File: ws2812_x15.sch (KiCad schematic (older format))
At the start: 16 parts

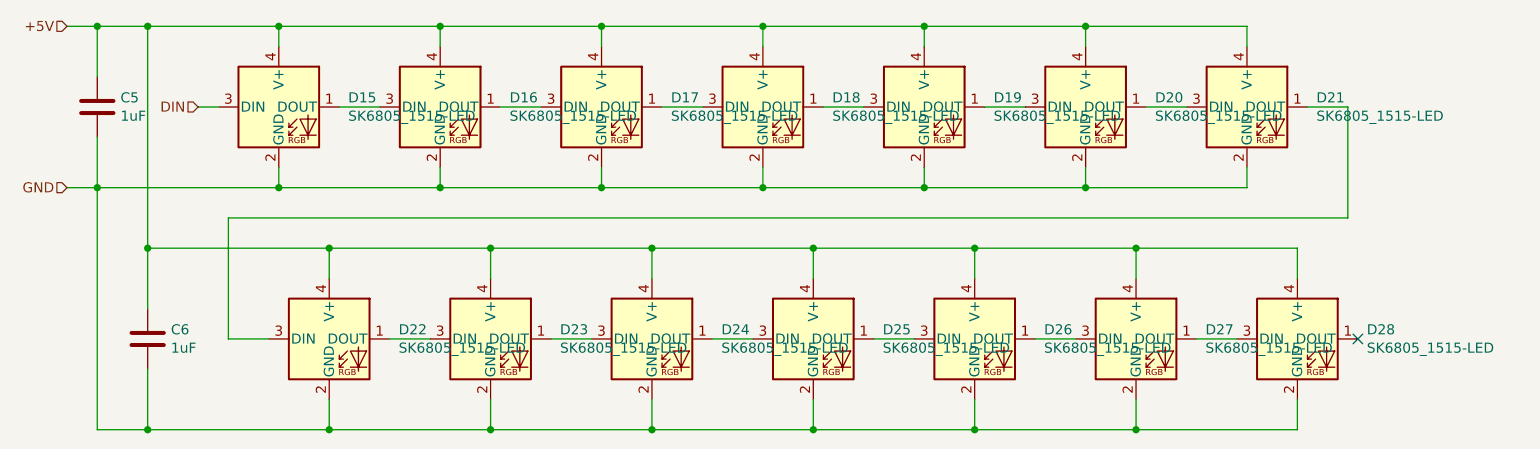
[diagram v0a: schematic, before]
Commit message: Update with changes to use attiny13a only
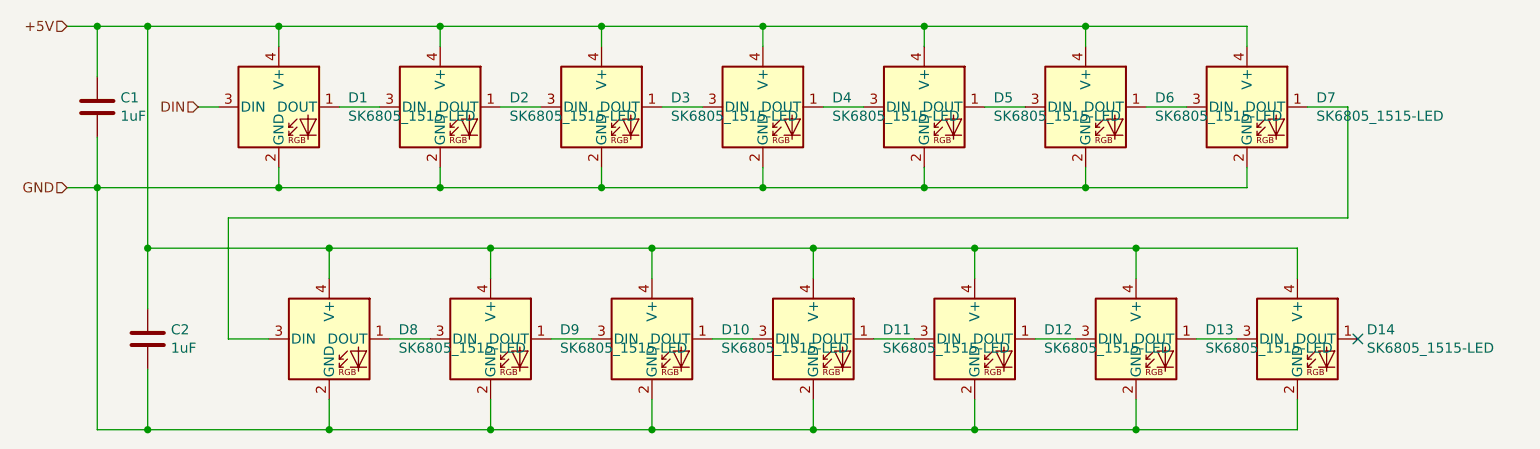
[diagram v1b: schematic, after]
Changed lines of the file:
@@
 $Descr A4 11693 8268
 encoding utf-8
-Sheet 1 3
+Sheet 2 3
 Title ""
 Date ""
@@
 AR Path="/5FC2CFBE/5FBCF9D4" Ref="D1"  Part="1"
 AR Path="/5FC2D616/5FBCF9D4" Ref="D15"  Part="1"
-AR Path="/5FC48FEB/5FBCF9D4" Ref="D?"  Part="1"
-AR Path="/5FC491DE/5FBCF9D4" Ref="D?"  Part="1"
-F 0 "D15" H 2794 1946 50  0000 L CNN
+AR Path="/5FC48FEB/5FBCF9D4" Ref="D1"  Part="1"
+AR Path="/5FC491DE/5FBCF9D4" Ref="D15"  Part="1"
+F 0 "D1" H 2794 1946 50  0000 L CNN
 F 1 "SK6805_1515-LED" H 2794 1855 50  0000 L CNN
 F 2 "LED_SMD:LED_SK6805_PLCC4_1.5x1.5mm_P0.65mm" H 2500 1600 50  0001 L TNN
@@
 AR Path="/5FC2CFBE/5FBD0769" Ref="C3"  Part="1"
 AR Path="/5FC2D616/5FBD0769" Ref="C5"  Part="1"
-AR Path="/5FC48FEB/5FBD0769" Ref="C?"  Part="1"
-AR Path="/5FC491DE/5FBD0769" Ref="C?"  Part="1"
-F 0 "C5" H 1665 1946 50  0000 L CNN
+AR Path="/5FC48FEB/5FBD0769" Ref="C1"  Part="1"
+AR Path="/5FC491DE/5FBD0769" Ref="C3"  Part="1"
+F 0 "C1" H 1665 1946 50  0000 L CNN
 F 1 "1uF" H 1665 1855 50  0000 L CNN
 F 2 "Capacitor_SMD:C_0603_1608Metric" H 1588 1750 50  0001 C CNN
@@
 AR Path="/5FC2CFBE/5FBD28C7" Ref="D2"  Part="1"
 AR Path="/5FC2D616/5FBD28C7" Ref="D16"  Part="1"
-AR Path="/5FC48FEB/5FBD28C7" Ref="D?"  Part="1"
-AR Path="/5FC491DE/5FBD28C7" Ref="D?"  Part="1"
-F 0 "D16" H 3594 1946 50  0000 L CNN
+AR Path="/5FC48FEB/5FBD28C7" Ref="D2"  Part="1"
+AR Path="/5FC491DE/5FBD28C7" Ref="D16"  Part="1"
+F 0 "D2" H 3594 1946 50  0000 L CNN
 F 1 "SK6805_1515-LED" H 3594 1855 50  0000 L CNN
 F 2 "LED_SMD:LED_SK6805_PLCC4_1.5x1.5mm_P0.65mm" H 3300 1600 50  0001 L TNN
@@
 AR Path="/5FC2CFBE/5FBD39DB" Ref="D3"  Part="1"
 AR Path="/5FC2D616/5FBD39DB" Ref="D17"  Part="1"
-AR Path="/5FC48FEB/5FBD39DB" Ref="D?"  Part="1"
-AR Path="/5FC491DE/5FBD39DB" Ref="D?"  Part="1"
-F 0 "D17" H 4394 1946 50  0000 L CNN
+AR Path="/5FC48FEB/5FBD39DB" Ref="D3"  Part="1"
+AR Path="/5FC491DE/5FBD39DB" Ref="D17"  Part="1"
+F 0 "D3" H 4394 1946 50  0000 L CNN
 F 1 "SK6805_1515-LED" H 4394 1855 50  0000 L CNN
 F 2 "LED_SMD:LED_SK6805_PLCC4_1.5x1.5mm_P0.65mm" H 4100 1600 50  0001 L TNN
@@
 AR Path="/5FC2CFBE/5FBD39E1" Ref="D4"  Part="1"
 AR Path="/5FC2D616/5FBD39E1" Ref="D18"  Part="1"
-AR Path="/5FC48FEB/5FBD39E1" Ref="D?"  Part="1"
-AR Path="/5FC491DE/5FBD39E1" Ref="D?"  Part="1"
-F 0 "D18" H 5194 1946 50  0000 L CNN
+AR Path="/5FC48FEB/5FBD39E1" Ref="D4"  Part="1"
+AR Path="/5FC491DE/5FBD39E1" Ref="D18"  Part="1"
+F 0 "D4" H 5194 1946 50  0000 L CNN
 F 1 "SK6805_1515-LED" H 5194 1855 50  0000 L CNN
 F 2 "LED_SMD:LED_SK6805_PLCC4_1.5x1.5mm_P0.65mm" H 4900 1600 50  0001 L TNN
@@
 AR Path="/5FC2CFBE/5FBD73F9" Ref="D5"  Part="1"
 AR Path="/5FC2D616/5FBD73F9" Ref="D19"  Part="1"
-AR Path="/5FC48FEB/5FBD73F9" Ref="D?"  Part="1"
-AR Path="/5FC491DE/5FBD73F9" Ref="D?"  Part="1"
-F 0 "D19" H 5994 1946 50  0000 L CNN
+AR Path="/5FC48FEB/5FBD73F9" Ref="D5"  Part="1"
+AR Path="/5FC491DE/5FBD73F9" Ref="D19"  Part="1"
+F 0 "D5" H 5994 1946 50  0000 L CNN
 F 1 "SK6805_1515-LED" H 5994 1855 50  0000 L CNN
 F 2 "LED_SMD:LED_SK6805_PLCC4_1.5x1.5mm_P0.65mm" H 5700 1600 50  0001 L TNN
@@
 AR Path="/5FC2CFBE/5FBD73FF" Ref="D6"  Part="1"
 AR Path="/5FC2D616/5FBD73FF" Ref="D20"  Part="1"
-AR Path="/5FC48FEB/5FBD73FF" Ref="D?"  Part="1"
-AR Path="/5FC491DE/5FBD73FF" Ref="D?"  Part="1"
-F 0 "D20" H 6794 1946 50  0000 L CNN
+AR Path="/5FC48FEB/5FBD73FF" Ref="D6"  Part="1"
+AR Path="/5FC491DE/5FBD73FF" Ref="D20"  Part="1"
+F 0 "D6" H 6794 1946 50  0000 L CNN
 F 1 "SK6805_1515-LED" H 6794 1855 50  0000 L CNN
 F 2 "LED_SMD:LED_SK6805_PLCC4_1.5x1.5mm_P0.65mm" H 6500 1600 50  0001 L TNN
@@
 AR Path="/5FC2CFBE/5FBD7405" Ref="D7"  Part="1"
 AR Path="/5FC2D616/5FBD7405" Ref="D21"  Part="1"
-AR Path="/5FC48FEB/5FBD7405" Ref="D?"  Part="1"
-AR Path="/5FC491DE/5FBD7405" Ref="D?"  Part="1"
-F 0 "D21" H 7594 1946 50  0000 L CNN
+AR Path="/5FC48FEB/5FBD7405" Ref="D7"  Part="1"
+AR Path="/5FC491DE/5FBD7405" Ref="D21"  Part="1"
+F 0 "D7" H 7594 1946 50  0000 L CNN
 F 1 "SK6805_1515-LED" H 7594 1855 50  0000 L CNN
 F 2 "LED_SMD:LED_SK6805_PLCC4_1.5x1.5mm_P0.65mm" H 7300 1600 50  0001 L TNN
@@
 AR Path="/5FC2CFBE/5FBDBDCA" Ref="D8"  Part="1"
 AR Path="/5FC2D616/5FBDBDCA" Ref="D22"  Part="1"
-AR Path="/5FC48FEB/5FBDBDCA" Ref="D?"  Part="1"
-AR Path="/5FC491DE/5FBDBDCA" Ref="D?"  Part="1"
-F 0 "D22" H 3044 3096 50  0000 L CNN
+AR Path="/5FC48FEB/5FBDBDCA" Ref="D8"  Part="1"
+AR Path="/5FC491DE/5FBDBDCA" Ref="D22"  Part="1"
+F 0 "D8" H 3044 3096 50  0000 L CNN
 F 1 "SK6805_1515-LED" H 3044 3005 50  0000 L CNN
 F 2 "LED_SMD:LED_SK6805_PLCC4_1.5x1.5mm_P0.65mm" H 2750 2750 50  0001 L TNN
@@
 AR Path="/5FC2CFBE/5FBDBDD0" Ref="D9"  Part="1"
 AR Path="/5FC2D616/5FBDBDD0" Ref="D23"  Part="1"
-AR Path="/5FC48FEB/5FBDBDD0" Ref="D?"  Part="1"
-AR Path="/5FC491DE/5FBDBDD0" Ref="D?"  Part="1"
-F 0 "D23" H 3844 3096 50  0000 L CNN
+AR Path="/5FC48FEB/5FBDBDD0" Ref="D9"  Part="1"
+AR Path="/5FC491DE/5FBDBDD0" Ref="D23"  Part="1"
+F 0 "D9" H 3844 3096 50  0000 L CNN
 F 1 "SK6805_1515-LED" H 3844 3005 50  0000 L CNN
 F 2 "LED_SMD:LED_SK6805_PLCC4_1.5x1.5mm_P0.65mm" H 3550 2750 50  0001 L TNN
@@
 AR Path="/5FC2CFBE/5FBDBDD6" Ref="D10"  Part="1"
 AR Path="/5FC2D616/5FBDBDD6" Ref="D24"  Part="1"
-AR Path="/5FC48FEB/5FBDBDD6" Ref="D?"  Part="1"
-AR Path="/5FC491DE/5FBDBDD6" Ref="D?"  Part="1"
-F 0 "D24" H 4644 3096 50  0000 L CNN
+AR Path="/5FC48FEB/5FBDBDD6" Ref="D10"  Part="1"
+AR Path="/5FC491DE/5FBDBDD6" Ref="D24"  Part="1"
+F 0 "D10" H 4644 3096 50  0000 L CNN
 F 1 "SK6805_1515-LED" H 4644 3005 50  0000 L CNN
 F 2 "LED_SMD:LED_SK6805_PLCC4_1.5x1.5mm_P0.65mm" H 4350 2750 50  0001 L TNN
@@
 AR Path="/5FC2CFBE/5FBDBDDC" Ref="D11"  Part="1"
 AR Path="/5FC2D616/5FBDBDDC" Ref="D25"  Part="1"
-AR Path="/5FC48FEB/5FBDBDDC" Ref="D?"  Part="1"
-AR Path="/5FC491DE/5FBDBDDC" Ref="D?"  Part="1"
-F 0 "D25" H 5444 3096 50  0000 L CNN
+AR Path="/5FC48FEB/5FBDBDDC" Ref="D11"  Part="1"
+AR Path="/5FC491DE/5FBDBDDC" Ref="D25"  Part="1"
+F 0 "D11" H 5444 3096 50  0000 L CNN
 F 1 "SK6805_1515-LED" H 5444 3005 50  0000 L CNN
 F 2 "LED_SMD:LED_SK6805_PLCC4_1.5x1.5mm_P0.65mm" H 5150 2750 50  0001 L TNN
@@
 AR Path="/5FC2CFBE/5FBDBDE2" Ref="D12"  Part="1"
 AR Path="/5FC2D616/5FBDBDE2" Ref="D26"  Part="1"
-AR Path="/5FC48FEB/5FBDBDE2" Ref="D?"  Part="1"
-AR Path="/5FC491DE/5FBDBDE2" Ref="D?"  Part="1"
-F 0 "D26" H 6244 3096 50  0000 L CNN
+AR Path="/5FC48FEB/5FBDBDE2" Ref="D12"  Part="1"
+AR Path="/5FC491DE/5FBDBDE2" Ref="D26"  Part="1"
+F 0 "D12" H 6244 3096 50  0000 L CNN
 F 1 "SK6805_1515-LED" H 6244 3005 50  0000 L CNN
 F 2 "LED_SMD:LED_SK6805_PLCC4_1.5x1.5mm_P0.65mm" H 5950 2750 50  0001 L TNN
@@
 AR Path="/5FC2CFBE/5FBDBDE8" Ref="D13"  Part="1"
 AR Path="/5FC2D616/5FBDBDE8" Ref="D27"  Part="1"
-AR Path="/5FC48FEB/5FBDBDE8" Ref="D?"  Part="1"
-AR Path="/5FC491DE/5FBDBDE8" Ref="D?"  Part="1"
-F 0 "D27" H 7044 3096 50  0000 L CNN
+AR Path="/5FC48FEB/5FBDBDE8" Ref="D13"  Part="1"
+AR Path="/5FC491DE/5FBDBDE8" Ref="D27"  Part="1"
+F 0 "D13" H 7044 3096 50  0000 L CNN
 F 1 "SK6805_1515-LED" H 7044 3005 50  0000 L CNN
 F 2 "LED_SMD:LED_SK6805_PLCC4_1.5x1.5mm_P0.65mm" H 6750 2750 50  0001 L TNN
@@
 AR Path="/5FC2CFBE/5FBDBDEE" Ref="D14"  Part="1"
 AR Path="/5FC2D616/5FBDBDEE" Ref="D28"  Part="1"
-AR Path="/5FC48FEB/5FBDBDEE" Ref="D?"  Part="1"
-AR Path="/5FC491DE/5FBDBDEE" Ref="D?"  Part="1"
-F 0 "D28" H 7844 3096 50  0000 L CNN
+AR Path="/5FC48FEB/5FBDBDEE" Ref="D14"  Part="1"
+AR Path="/5FC491DE/5FBDBDEE" Ref="D28"  Part="1"
+F 0 "D14" H 7844 3096 50  0000 L CNN
 F 1 "SK6805_1515-LED" H 7844 3005 50  0000 L CNN
 F 2 "LED_SMD:LED_SK6805_PLCC4_1.5x1.5mm_P0.65mm" H 7550 2750 50  0001 L TNN
@@
 AR Path="/5FC2CFBE/5FBDD238" Ref="C4"  Part="1"
 AR Path="/5FC2D616/5FBDD238" Ref="C6"  Part="1"
-AR Path="/5FC48FEB/5FBDD238" Ref="C?"  Part="1"
-AR Path="/5FC491DE/5FBDD238" Ref="C?"  Part="1"
-F 0 "C6" H 1915 3096 50  0000 L CNN
+AR Path="/5FC48FEB/5FBDD238" Ref="C2"  Part="1"
+AR Path="/5FC491DE/5FBDD238" Ref="C4"  Part="1"
+F 0 "C2" H 1915 3096 50  0000 L CNN
 F 1 "1uF" H 1915 3005 50  0000 L CNN
 F 2 "Capacitor_SMD:C_0603_1608Metric" H 1838 2900 50  0001 C CNN
